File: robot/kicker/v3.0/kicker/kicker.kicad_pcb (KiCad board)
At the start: 2 copper layers, 55 x 110 mm, 220 parts, among them J1 XT30-F, J10 Conn_01x10, J11 Conn_01x06, J12 Conn_01x02, J13 Conn_01x02, J2 Conn_ARM_JTAG_SWD_10, J3 Conn_01x10, J4 Conn_01x10, J5 Conn_01x02, J6 Conn_01x02, J7 Conn_01x10, J8 Conn_01x03, J9 Conn_01x03, Q1 BSS138, Q2 SQJA80EP-T1_GE3, Q3 SQJA80EP-T1_GE3, Q4 BSS138K, Q5 IXGA48N60A3, Q6 IXGA48N60A3, Q7 BSC0402NSATMA1, SW1 PWR_ON, SW2 RST, SW3 BTN0, SW4 SW_DIP_x04, U1 LTC4367, U10 IX4427, U11 LT3757EMSE, U12 AT25DF041x-UxN-x, U13 AD8494, U2 LTC2955-1, U3 LT3504, U4 STM32F411RETx, U5 SK9822, U6 SK9822, U7 ISO6720-Q1, U8 ISO6721-Q1, U9 ISO6720-Q1

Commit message: kicker v3.0 layout work
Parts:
- F1, R49: moved to F.Cu
- moved Q7 355.7 mm to (241.2, 132.5), turned to 90 degrees
- moved R63 348.7 mm to (241.0, 138.5), turned to 90 degrees
- moved R62 346.3 mm to (238.5, 138.5), turned to 90 degrees
- moved C1 255.6 mm to (235.5, 116.0), turned to 90 degrees
- moved R2 246.4 mm to (222.0, 105.0), turned to 90 degrees
- moved R1 240.6 mm to (217.0, 105.0), turned to 90 degrees
- moved C2 232.8 mm to (212.5, 117.5), turned to 90 degrees
- moved R49 28.1 mm to (200.5, 195.0), turned to 0 degrees
- moved U7 26.0 mm to (205.6, 192.3)
- moved U8 25.3 mm to (210.6, 192.3)
- moved U9 22.3 mm to (215.7, 192.3)
- moved C28 22.3 mm to (220.5, 190.2)
- moved C29 22.3 mm to (220.5, 192.1)
- moved C30 22.3 mm to (220.5, 194.1)
- moved C31 22.3 mm to (220.5, 196.1)
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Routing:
- net /hv_kicker/flyback_charger/V_{trans}: track 0.00 -> 2.33 mm, vias 0 -> 42
- net /hv_kicker/flyback_charger/V_{solenoid}: vias 0 -> 9
- added copper zone on B.Cu, net +BATT
- added copper zone on F.Cu, net /hv_kicker/flyback_charger/CSP
- added copper zone on B.Cu, net /hv_kicker/flyback_charger/HV_AC
- added copper zone on B.Cu, net /hv_kicker/flyback_charger/V_{solenoid}
- added copper zone on F.Cu, net /hv_kicker/flyback_charger/V_{solenoid}
- added copper zone on B.Cu, net /hv_kicker/flyback_charger/V_{trans}
- added copper zone on F.Cu, net /hv_kicker/flyback_charger/V_{trans}
- added copper zone on F.Cu, net /hv_kicker/solenoid_control/CHIP_SW
- added copper zone on F.Cu, net /hv_kicker/solenoid_control/KICK_SW
- added copper zone on B.Cu, net GND
- added copper zone on F.Cu, net GND
- added copper zone on In1.Cu, net GND
- added copper zone on In2.Cu, net GND
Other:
- board size 55 x 110 mm -> 90 x 110 mm
- copper layers 2 -> 4

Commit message: kicker v3.0 layout work
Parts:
- F1: footprint Fuse:Fuse_Littelfuse-NANO2-451_453 -> AT-Fuses:3557-2; moved to B.Cu
- moved C39 356.9 mm to (253.5, 133.9), turned to 180 degrees
- moved C42 356.2 mm to (252.6, 140.4), turned to -90 degrees
- moved C45 355.0 mm to (251.5, 142.4), turned to -90 degrees
- moved C43 351.0 mm to (247.5, 140.0)
- moved R64 346.9 mm to (254.9, 143.4), turned to -90 degrees
- moved TP9 346.9 mm to (258.1, 143.9), turned to -90 degrees
- moved TP8 346.9 mm to (258.1, 140.3), turned to -90 degrees
- moved R65 346.7 mm to (254.9, 141.4), turned to -90 degrees
- moved R66 346.6 mm to (254.9, 139.3), turned to -90 degrees
- moved R57 344.5 mm to (252.5, 135.0)
- moved R58 343.7 mm to (251.5, 140.4), turned to 90 degrees
- moved U11 339.6 mm to (250.2, 137.5), turned to 180 degrees
- moved C40 337.8 mm to (247.0, 142.0)
- moved R60 336.9 mm to (245.0, 137.1)
- moved R61 336.8 mm to (245.0, 136.1), turned to 180 degrees
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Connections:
- net Net-(Q2-D) renamed /Power Protection/V_{BATT}_FUSED
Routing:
- net /hv_kicker/flyback_charger/FB: track 0.00 -> 8.17 mm
- net /digital/CMD_{CHG}: track 0.00 -> 7.50 mm
- net Net-(Q7-G): track 0.00 -> 6.92 mm
- net Net-(U11-SS): track 0.00 -> 5.35 mm
- net +BATT: track 0.00 -> 5.04 mm
- net /hv_kicker/flyback_charger/CSP: track 0.00 -> 4.40 mm
- net Net-(U11-RT): track 0.00 -> 3.65 mm
- net /hv_kicker/flyback_charger/HVGATE: track 0.00 -> 3.62 mm
- net GND: track 0.00 -> 3.54 mm, vias 0 -> 27
- net Net-(U11-VC): track 0.00 -> 3.07 mm
- net +12V: track 0.00 -> 3.03 mm
- net Net-(C45-Pad1): track 0.00 -> 1.01 mm
- added copper zone on B.Cu, net /Power Protection/V_{BATT}
- added copper zone on F.Cu, net /Power Protection/V_{BATT}
- added copper zone on In1.Cu, net /Power Protection/V_{BATT}
- added copper zone on In2.Cu, net /Power Protection/V_{BATT}
- added copper zone on F.Cu, net /Power Protection/V_{BATT}_FUSED
- added copper zone on F.Cu, net Net-(C1-Pad2)

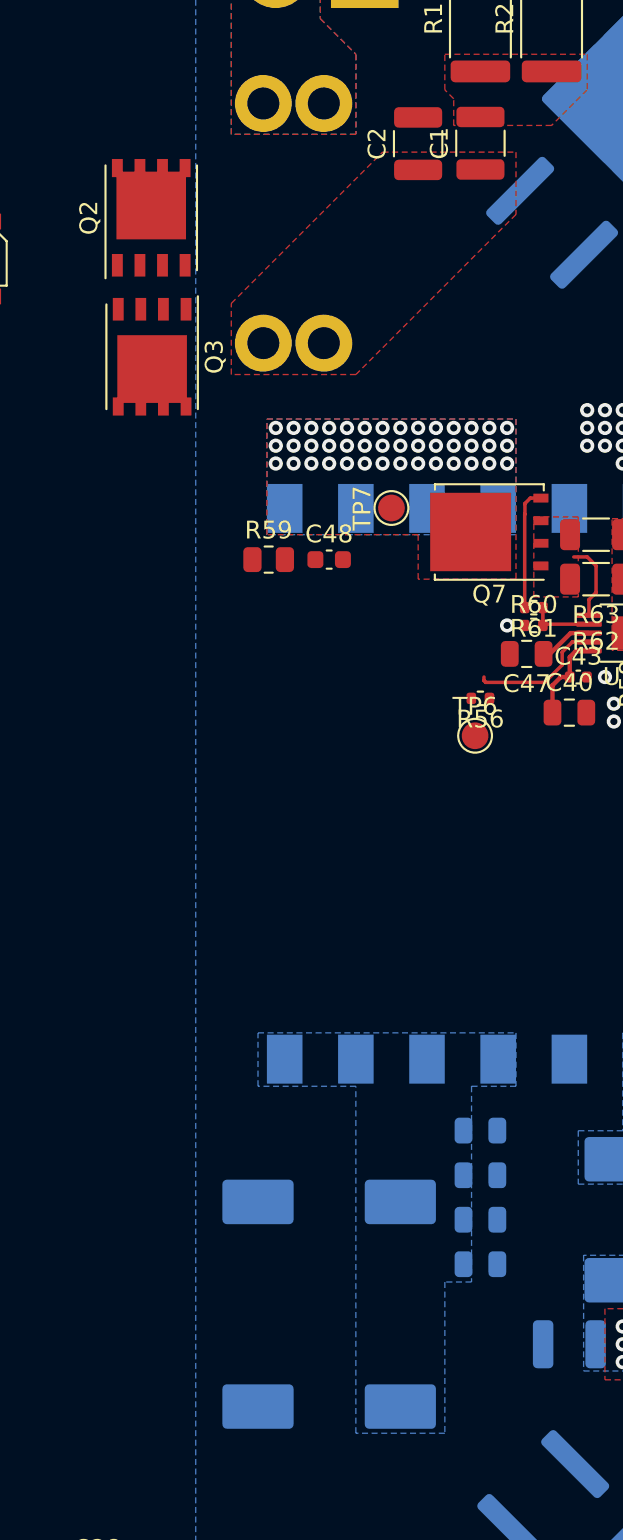
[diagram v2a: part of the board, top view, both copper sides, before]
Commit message: fix HV net class spacing rules
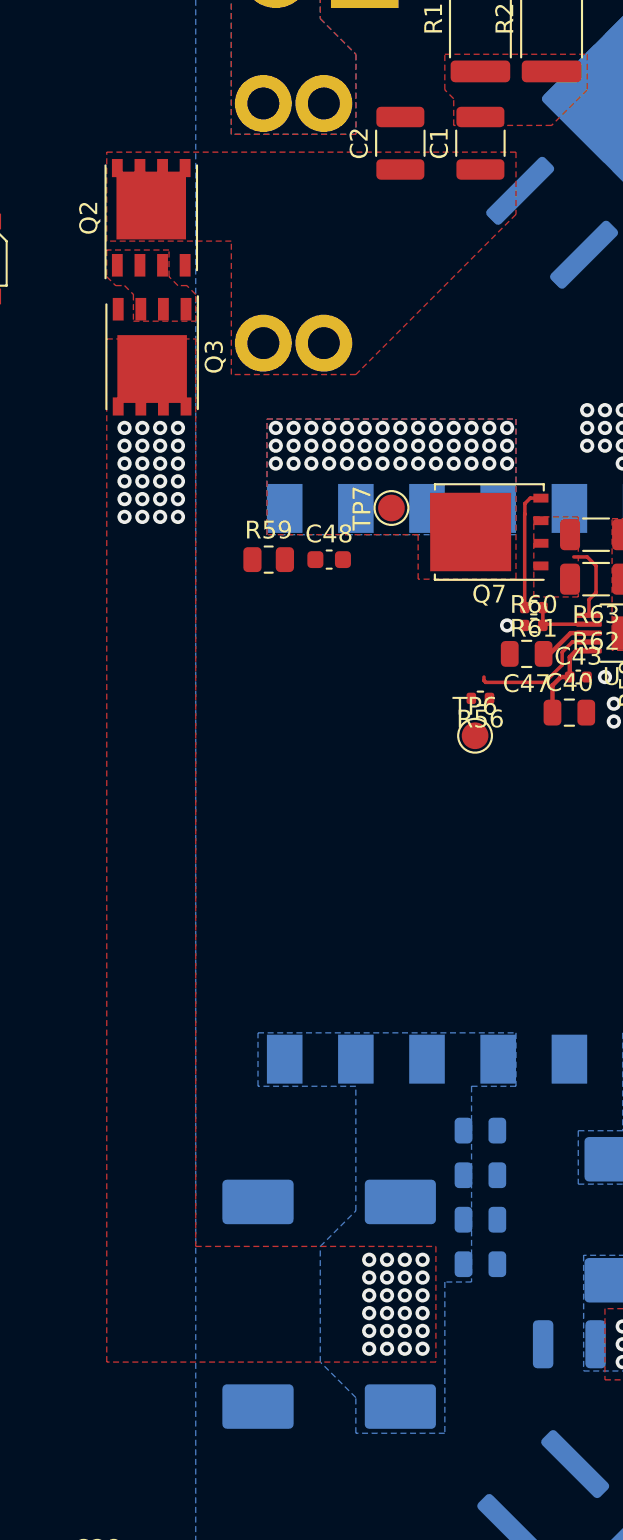
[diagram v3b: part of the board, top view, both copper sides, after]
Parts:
- moved C2 1.00 mm to (237.5, 110.0)
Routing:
- net +BATT: vias 0 -> 48
- added copper zone on F.Cu, net +BATT
- added copper zone on In1.Cu, net +BATT
- added copper zone on F.Cu, net Net-(Q2-S-Pad1)
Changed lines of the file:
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@@
   )
   (footprint "Capacitor_SMD:C_1210_3225Metric" (layer "F.Cu")
-    (at 238.5 110.025 90)
+    (at 237.5 110 90)
     (descr "Capacitor SMD 1210 (3225 Metric), square (rectangular) end terminal, IPC_7351 nominal, (Body size source: IPC-SM-782 page 76, https://www.pcb-3d.com/wordpress/wp-content/uploads/ipc-sm-782a_amendment_1_and_2.pdf), generated with kicad-footprint-generator")
     (tags "capacitor")
@@
   (segment (start 248.1 138.53) (end 247.37 138.53) (width 0.25) (layer "F.Cu") (net 16))
   (segment (start 246.05 142) (end 246.05 140.47) (width 0.25) (layer "F.Cu") (net 16))
+  (via (at 224 131) (size 0.8) (drill 0.4) (layers "F.Cu" "B.Cu") (free) (net 16))
+  (via (at 238.75 176.75) (size 0.8) (drill 0.4) (layers "F.Cu" "B.Cu") (free) (net 16))
+  (via (at 236.75 177.75) (size 0.8) (drill 0.4) (layers "F.Cu" "B.Cu") (free) (net 16))
+  (via (at 225 129) (size 0.8) (drill 0.4) (layers "F.Cu" "B.Cu") (free) (net 16))
+  (via (at 237.75 176.75) (size 0.8) (drill 0.4) (layers "F.Cu" "B.Cu") (free) (net 16))
+  (via (at 223 127) (size 0.8) (drill 0.4) (layers "F.Cu" "B.Cu") (free) (net 16))
+  (via (at 238.75 177.75) (size 0.8) (drill 0.4) (layers "F.Cu" "B.Cu") (free) (net 16))
+  (via (at 222 131) (size 0.8) (drill 0.4) (layers "F.Cu" "B.Cu") (free) (net 16))
+  (via (at 237.75 173.75) (size 0.8) (drill 0.4) (layers "F.Cu" "B.Cu") (free) (net 16))
+  (via (at 224 129) (size 0.8) (drill 0.4) (layers "F.Cu" "B.Cu") (free) (net 16))
+  (via (at 224 126) (size 0.8) (drill 0.4) (layers "F.Cu" "B.Cu") (free) (net 16))
+  (via (at 236.75 172.75) (size 0.8) (drill 0.4) (layers "F.Cu" "B.Cu") (free) (net 16))
+  (via (at 237.75 174.75) (size 0.8) (drill 0.4) (layers "F.Cu" "B.Cu") (free) (net 16))
+  (via (at 222 130) (size 0.8) (drill 0.4) (layers "F.Cu" "B.Cu") (free) (net 16))
+  (via (at 235.75 174.75) (size 0.8) (drill 0.4) (layers "F.Cu" "B.Cu") (free) (net 16))
+  (via (at 225 130) (size 0.8) (drill 0.4) (layers "F.Cu" "B.Cu") (free) (net 16))
+  (via (at 222 128) (size 0.8) (drill 0.4) (layers "F.Cu" "B.Cu") (free) (net 16))
+  (via (at 224 127) (size 0.8) (drill 0.4) (layers "F.Cu" "B.Cu") (free) (net 16))
+  (via (at 235.75 173.75) (size 0.8) (drill 0.4) (layers "F.Cu" "B.Cu") (free) (net 16))
+  (via (at 235.75 172.75) (size 0.8) (drill 0.4) (layers "F.Cu" "B.Cu") (free) (net 16))
+  (via (at 223 131) (size 0.8) (drill 0.4) (layers "F.Cu" "B.Cu") (free) (net 16))
+  (via (at 238.75 175.75) (size 0.8) (drill 0.4) (layers "F.Cu" "B.Cu") (free) (net 16))
+  (via (at 238.75 174.75) (size 0.8) (drill 0.4) (layers "F.Cu" "B.Cu") (free) (net 16))
+  (via (at 225 126) (size 0.8) (drill 0.4) (layers "F.Cu" "B.Cu") (free) (net 16))
+  (via (at 224 130) (size 0.8) (drill 0.4) (layers "F.Cu" "B.Cu") (free) (net 16))
+  (via (at 223 128) (size 0.8) (drill 0.4) (layers "F.Cu" "B.Cu") (free) (net 16))
+  (via (at 235.75 175.75) (size 0.8) (drill 0.4) (layers "F.Cu" "B.Cu") (free) (net 16))
+  (via (at 225 128) (size 0.8) (drill 0.4) (layers "F.Cu" "B.Cu") (free) (net 16))
+  (via (at 235.75 177.75) (size 0.8) (drill 0.4) (layers "F.Cu" "B.Cu") (free) (net 16))
+  (via (at 236.75 176.75) (size 0.8) (drill 0.4) (layers "F.Cu" "B.Cu") (free) (net 16))
+  (via (at 236.75 175.75) (size 0.8) (drill 0.4) (layers "F.Cu" "B.Cu") (free) (net 16))
+  (via (at 223 129) (size 0.8) (drill 0.4) (layers "F.Cu" "B.Cu") (free) (net 16))
+  (via (at 238.75 172.75) (size 0.8) (drill 0.4) (layers "F.Cu" "B.Cu") (free) (net 16))
+  (via (at 236.75 173.75) (size 0.8) (drill 0.4) (layers "F.Cu" "B.Cu") (free) (net 16))
+  (via (at 222 129) (size 0.8) (drill 0.4) (layers "F.Cu" "B.Cu") (free) (net 16))
+  (via (at 237.75 177.75) (size 0.8) (drill 0.4) (layers "F.Cu" "B.Cu") (free) (net 16))
+  (via (at 237.75 172.75) (size 0.8) (drill 0.4) (layers "F.Cu" "B.Cu") (free) (net 16))
+  (via (at 236.75 174.75) (size 0.8) (drill 0.4) (layers "F.Cu" "B.Cu") (free) (net 16))
+  (via (at 225 131) (size 0.8) (drill 0.4) (layers "F.Cu" "B.Cu") (free) (net 16))
+  (via (at 223 130) (size 0.8) (drill 0.4) (layers "F.Cu" "B.Cu") (free) (net 16))
+  (via (at 225 127) (size 0.8) (drill 0.4) (layers "F.Cu" "B.Cu") (free) (net 16))
+  (via (at 222 126) (size 0.8) (drill 0.4) (layers "F.Cu" "B.Cu") (free) (net 16))
+  (via (at 223 126) (size 0.8) (drill 0.4) (layers "F.Cu" "B.Cu") (free) (net 16))
+  (via (at 237.75 175.75) (size 0.8) (drill 0.4) (layers "F.Cu" "B.Cu") (free) (net 16))
+  (via (at 235.75 176.75) (size 0.8) (drill 0.4) (layers "F.Cu" "B.Cu") (free) (net 16))
+  (via (at 222 127) (size 0.8) (drill 0.4) (layers "F.Cu" "B.Cu") (free) (net 16))
+  (via (at 224 128) (size 0.8) (drill 0.4) (layers "F.Cu" "B.Cu") (free) (net 16))
+  (via (at 238.75 173.75) (size 0.8) (drill 0.4) (layers "F.Cu" "B.Cu") (free) (net 16))
   (via (at 252 178.5) (size 0.8) (drill 0.4) (layers "F.Cu" "B.Cu") (free) (net 21))
   (via (at 252 177.5) (size 0.8) (drill 0.4) (layers "F.Cu" "B.Cu") (free) (net 21))
@@
   (zone (net 1) (net_name "/Power Protection/V_{BATT}_FUSED") (layer "F.Cu") (hatch edge 0.5)
     (priority 9)
-    (connect_pads yes (clearance 1))
+    (connect_pads yes (clearance 0.25))
     (min_thickness 0.25) (filled_areas_thickness no)
     (fill yes (thermal_gap 0.5) (thermal_bridge_width 0.5))
@@
         (xy 235 123)
         (xy 228 123)
-        (xy 228 119)
-        (xy 236.5 110.5)
+        (xy 228 115.5)
+        (xy 221 115.5)
+        (xy 221 110.5)
         (xy 244 110.5)
         (xy 244 114)
@@
     )
   )
+  (zone (net 107) (net_name "Net-(Q2-S-Pad1)") (layer "F.Cu") (hatch edge 0.5)
+    (priority 12)
+    (connect_pads yes (clearance 0.25))
+    (min_thickness 0.25) (filled_areas_thickness no)
+    (fill yes (thermal_gap 0.5) (thermal_bridge_width 0.5))
+    (polygon
+      (pts
+        (xy 226 120)
+        (xy 226 118.5)
+        (xy 225.5 118)
+        (xy 225 118)
+        (xy 224.5 117.5)
+        (xy 224.5 116)
+        (xy 221 116)
+        (xy 221 117.5)
+        (xy 221.5 118)
+        (xy 222 118)
+        (xy 222.5 118.5)
+        (xy 222.5 120)
+      )
+    )
+  )
   (zone (net 3) (net_name "GND") (layer "F.Cu") (hatch edge 0.5)
     (priority 4)
@@
     )
   )
+  (zone (net 16) (net_name "+BATT") (layers "F.Cu" "In1.Cu") (hatch edge 0.5)
+    (priority 13)
+    (connect_pads yes (clearance 0.25))
+    (min_thickness 0.25) (filled_areas_thickness no)
+    (fill yes (thermal_gap 0.5) (thermal_bridge_width 0.5))
+    (polygon
+      (pts
+        (xy 226 121)
+        (xy 226 172)
+        (xy 239.5 172)
+        (xy 239.5 178.5)
+        (xy 221 178.5)
+        (xy 221 121)
+      )
+    )
+  )
   (zone (net 3) (net_name "GND") (layers "F.Cu" "In1.Cu" "In2.Cu") (hatch edge 0.5)
     (connect_pads yes (clearance 0.25))
@@
   )
   (zone (net 3) (net_name "GND") (layer "B.Cu") (hatch edge 0.5)
-    (connect_pads yes (clearance 1))
+    (connect_pads yes (clearance 0.25))
     (min_thickness 0.25) (filled_areas_thickness no)
     (fill yes (thermal_gap 0.5) (thermal_bridge_width 0.5))
@@
         (xy 240 182.5)
         (xy 235 182.5)
+        (xy 235 180.5)
+        (xy 233 178.5)
+        (xy 233 172)
+        (xy 235 170)
         (xy 235 163)
         (xy 229.5 163)

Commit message: kicker v3.0 changes from design review
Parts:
- removed C10: 47n 6.3V, Capacitor_SMD:C_0402_1005Metric
- removed JP8: TRIM_DISABLE, AT-BoardFeatures:SolderJumper-2_2.0x1.2mm_Closed
- removed RV1: 500, Potentiometer_THT:Potentiometer_Bourns_3386X_Horizontal
- added Ce1: 470n 6.3V, Capacitor_SMD:C_0402_1005Metric, F.Cu at (-114.3, 88.2)
- added R74: 2.1k, Resistor_SMD:R_0402_1005Metric, F.Cu at (-119.2, 82.3)
- added R75: 2.1k, Resistor_SMD:R_0402_1005Metric, F.Cu at (-119.2, 84.2)
- added R76: 10k, Resistor_SMD:R_0402_1005Metric, F.Cu at (-114.3, 82.3)
- added R77: 10k, Resistor_SMD:R_0402_1005Metric, F.Cu at (-114.3, 84.2)
- C11: value 1u 25V -> 1u 50V
- C12, C54: value 1u 6.3V -> 1u 50V
- C13: value 1u 10V -> 1u 50V
- C14: value 1u 16V -> 1u 50V
- C16: value 10u 6.3V -> 10u 25V
- C17: value 10u 10V -> 10u 25V
- C18: value 10u 16V -> 10u 25V
- C34: value 10u 50v -> 10u 50V
- C9: value 47n 6.3V -> 470n 6.3V
- D1: value 824521481 -> 824521261
- D10: value Yellow -> Red
- L1: value 744773122 -> ASPI-6045S-220M-T
- L2: value 784773068 -> SDCHA1V5040-150-R
- L3: value 74477310 -> SDCHA1V5040-150-R
- L4: value 744773112 -> SDCHA1V5040-150-R
- L5: value 744773082 -> SDCHA1V5040-150-R
- R3, R42, R43, R44, R45, R46, R47, R64, R65: footprint Resistor_SMD:R_0402_1005Metric -> Resistor_SMD:R_0805_2012Metric
- moved R49 6.17 mm to (206.2, 197.2)
- moved C28 5.04 mm to (225.5, 190.7)
- moved C29 5.04 mm to (225.5, 192.6)
- moved C30 5.04 mm to (225.5, 194.6)
- moved C31 5.04 mm to (225.5, 196.6)
- moved C32 5.04 mm to (225.5, 198.5)
- moved C33 5.04 mm to (225.5, 200.5)
- moved U8 5.04 mm to (215.7, 192.8)
- moved U9 5.04 mm to (220.7, 192.8)
- moved U7 5.04 mm to (210.6, 192.8)
- moved U1 3.92 mm to (217.5, 118.0)
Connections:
- net /Ball Sense/SENSE_BOOT_UART.~{RST} renamed /Ball Sense/SENSE_BOOT_UART.RST
- net /Dribbler/DRIB_BOOT_UART.~{RST} renamed /Dribbler/DRIB_BOOT_UART.RST
- net /digital/MCU_BOOT_UART.~{RST} renamed /digital/MCU_BOOT_UART.RST
- net /isol/BOOT_UART_~{RST}_ISOL renamed /isol/BOOT_UART_RST_ISOL
- J8 pad 1: Net-(J8-Pin_1) -> +3V3
- R37 pad 1: +3V3 -> GND
- R38 pad 1: +3V3 -> GND
- R39 pad 1: +3V3 -> GND
- R40 pad 1: +3V3 -> GND
- SW4 pad 5: GND -> +3V3
- SW4 pad 6: GND -> +3V3
- SW4 pad 7: GND -> +3V3
- SW4 pad 8: GND -> +3V3

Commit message: finish schematic fixes from the design review, layout work
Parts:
- added D16: PESD3V3L5UY, Package_TO_SOT_SMD:SOT-363_SC-70-6, F.Cu at (-97.7, 68.1)
- C22, C23, C28, C29, C30, C31, C32, C33, C5, C52, C53, C57, C58, C59, C60, C61, C65: value 100n 6.3V -> 100n 50V
- C4: value 100n 10V -> 100n 50V
- L1: footprint AT-Inductors:WE-744773XXX-4.5mm_4.0mm -> AT-Inductors:ASPI-6045S
- L2, L3, L4, L5: footprint AT-Inductors:WE-744773XXX-4.5mm_4.0mm -> AT-Inductors:SDCHA1V50
- R3, R42, R43, R44, R45: value 1M47 -> 1.47M
- R48: value 4k75 -> 4.75k
- R59: value 1 1% -> 1
- R60: value 100k 1% -> 100k
- R61: value 10 1% -> 10
- R62, R63: value 4m00 1% -> 4m 1%
- R64, R65: value 976k 0%1 -> 976k 0.1%
- R66: value 17k4 0%1 -> 17.4k 0.1%
- moved SW2 299.9 mm to (217.7, 201.1)
- moved SW3 289.0 mm to (208.1, 201.1)
- moved SW4 278.2 mm to (209.8, 191.2), turned to -90 degrees
- moved SW1 243.7 mm to (221.6, 100.3)
- moved J8 40.4 mm to (-78.0, 167.6)
- moved J9 30.5 mm to (-64.8, 168.3), turned to -90 degrees
- moved C28 21.7 mm to (247.2, 190.4)
- moved C29 21.7 mm to (247.2, 192.3)
- moved C30 21.7 mm to (247.2, 194.3)
- moved C31 21.7 mm to (247.2, 196.3)
- moved C32 21.7 mm to (247.2, 198.3)
- moved C33 21.7 mm to (247.2, 200.2)
- moved J4 18.2 mm to (230.7, 201.4)
- moved R49 17.1 mm to (223.0, 200.9), turned to 90 degrees
- moved U9 14.5 mm to (235.2, 192.6)
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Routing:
- net +BATT: track 5.04 -> 17.2 mm
- net /isol/BOOT_UART_RST_ISOL: track 0.00 -> 4.36 mm
- net /isol/BOOT_UART_BOOT0_ISOL: track 0.00 -> 4.25 mm
- net /hv_kicker/flyback_charger/V_{trans}: track 2.33 -> 4.78 mm
- net /hv_kicker/flyback_charger/V_{solenoid}: track 0.00 -> 2.31 mm
- net Net-(C48-Pad1): track 0.00 -> 2.00 mm
- net /hv_kicker/flyback_charger/HVFBS: track 0.00 -> 1.77 mm
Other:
- board size 90 x 110 mm -> 113 x 110 mm

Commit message: layout work
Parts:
- R15: footprint Resistor_SMD:R_0603_1608Metric -> Resistor_SMD:R_0402_1005Metric
- moved R76 327.9 mm to (211.5, 119.2), turned to -90 degrees
- moved R77 321.8 mm to (206.2, 111.8)
- moved R15 260.3 mm to (218.8, 119.5), turned to -90 degrees
- moved D1 259.0 mm to (220.5, 107.5), turned to 180 degrees
- moved JP2 257.2 mm to (212.2, 123.2)
- moved JP1 257.2 mm to (212.2, 121.5)
- moved D3 254.4 mm to (216.8, 129.2)
- moved R12 251.3 mm to (220.0, 116.8), turned to -90 degrees
- moved R9 247.7 mm to (216.5, 112.0), turned to -90 degrees
- moved R13 247.1 mm to (220.0, 119.5), turned to -90 degrees
- moved R10 246.4 mm to (215.0, 112.5), turned to 180 degrees
- moved D2 245.9 mm to (208.5, 129.2), turned to 180 degrees
- moved R11 244.7 mm to (213.0, 112.5)
- moved Q1 242.6 mm to (202.0, 121.5), turned to 90 degrees
- moved R4 239.5 mm to (207.0, 126.2)
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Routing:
- net /Power Protection/V_{BATT}_FUSED: track 0.00 -> 31.9 mm, vias 0 -> 2
- net Net-(Q1-D): track 0.00 -> 31.8 mm
- net /isol/CLK_32K_ISOL: track 0.00 -> 13.9 mm
- net /isol/CLK_8M_ISOL: track 0.00 -> 13.7 mm
- net Net-(D2-A2): track 0.00 -> 12.5 mm
- net +BATT: track 17.2 -> 29.4 mm
- net /isol/V_{logic}_ISOL: track 0.00 -> 10.8 mm, vias 0 -> 4
- net /isol/GND_ISOL: track 0.00 -> 10.0 mm, vias 0 -> 7
- net Net-(D1-A2): track 0.00 -> 9.86 mm
- net Net-(Q2-G): track 0.00 -> 9.75 mm, vias 0 -> 2
- net /isol/BOOT_UART_RX_ISOL: track 0.00 -> 8.34 mm
- net /isol/BOOT_UART_TX_ISOL: track 0.00 -> 8.23 mm
- net /digital/MCU_BOOT_UART.~{DET}: track 0.00 -> 7.95 mm
- net +3V3: track 0.00 -> 7.04 mm, vias 0 -> 2
- net Net-(U1-GATE): track 0.00 -> 5.50 mm
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- added copper zone on B.Cu, net /isol/GND_ISOL
- added copper zone on F.Cu, net /isol/GND_ISOL
- added copper zone on In2.Cu, net /isol/GND_ISOL
- added copper zone on In1.Cu, net /isol/V_{logic}_ISOL
